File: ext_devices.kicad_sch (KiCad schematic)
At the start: 12 parts, among them CON1 MIKROBUS_HOST_CONN, J14 Conn_01x08_Female, J15 Conn_01x08_Female, U12 TXS0102DCU, U13 TXS0102DCU

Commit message: optimized component selection, assigned missing LCSC part numbers
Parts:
- C61, C62, C63, C64: footprint Capacitor_SMD:C_0805_2012Metric_Pad1.18x1.45mm_HandSolder -> Capacitor_SMD:C_0805_2012Metric
- D3: LCSC (none) -> C96235
- U12, U13: LCSC (none) -> C53434
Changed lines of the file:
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@@
     (property "Reference" "C64" (id 0) (at 130.81 128.27 90))
     (property "Value" "100nF" (id 1) (at 130.81 130.81 90))
-    (property "Footprint" "Capacitor_SMD:C_0805_2012Metric_Pad1.18x1.45mm_HandSolder" (id 2) (at 134.62 134.9248 0)
+    (property "Footprint" "Capacitor_SMD:C_0805_2012Metric" (id 2) (at 134.62 134.9248 0)
       (effects (font (size 1.27 1.27)) hide)
     )
@@
     (property "Reference" "C63" (id 0) (at 118.11 128.27 90))
     (property "Value" "100nF" (id 1) (at 118.11 130.81 90))
-    (property "Footprint" "Capacitor_SMD:C_0805_2012Metric_Pad1.18x1.45mm_HandSolder" (id 2) (at 121.92 134.9248 0)
+    (property "Footprint" "Capacitor_SMD:C_0805_2012Metric" (id 2) (at 121.92 134.9248 0)
       (effects (font (size 1.27 1.27)) hide)
     )
@@
     (property "Reference" "C62" (id 0) (at 62.865 128.27 90))
     (property "Value" "100nF" (id 1) (at 62.865 130.81 90))
-    (property "Footprint" "Capacitor_SMD:C_0805_2012Metric_Pad1.18x1.45mm_HandSolder" (id 2) (at 66.675 134.9248 0)
+    (property "Footprint" "Capacitor_SMD:C_0805_2012Metric" (id 2) (at 66.675 134.9248 0)
       (effects (font (size 1.27 1.27)) hide)
     )
@@
     )
     (property "Datasheet" "http://www.ti.com/lit/gpn/txs0102" (id 3) (at 124.46 152.908 0)
+      (effects (font (size 1.27 1.27)) hide)
+    )
+    (property "LCSC" "C53434" (id 4) (at 124.46 152.4 0)
       (effects (font (size 1.27 1.27)) hide)
     )
@@
     (property "Reference" "C61" (id 0) (at 45.085 128.27 90))
     (property "Value" "100nF" (id 1) (at 45.085 130.81 90))
-    (property "Footprint" "Capacitor_SMD:C_0805_2012Metric_Pad1.18x1.45mm_HandSolder" (id 2) (at 48.895 134.9248 0)
+    (property "Footprint" "Capacitor_SMD:C_0805_2012Metric" (id 2) (at 48.895 134.9248 0)
       (effects (font (size 1.27 1.27)) hide)
     )
@@
     )
     (property "Datasheet" "https://datasheet.lcsc.com/lcsc/1811061814_Nexperia-PMEG4050EP-115_C96235.pdf" (id 3) (at 192.405 36.83 0)
+      (effects (font (size 1.27 1.27)) hide)
+    )
+    (property "LCSC" "C96235" (id 4) (at 192.405 36.83 0)
       (effects (font (size 1.27 1.27)) hide)
     )
@@
       (effects (font (size 1.27 1.27)) hide)
     )
+    (property "LCSC" "C53434" (id 4) (at 53.34 152.4 0)
+      (effects (font (size 1.27 1.27)) hide)
+    )

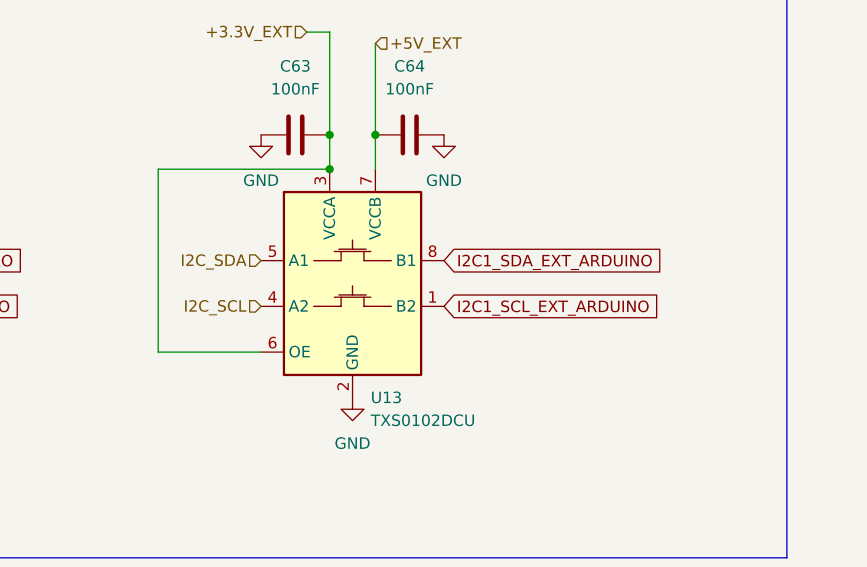
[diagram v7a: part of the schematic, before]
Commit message: added second level shifter to PCB
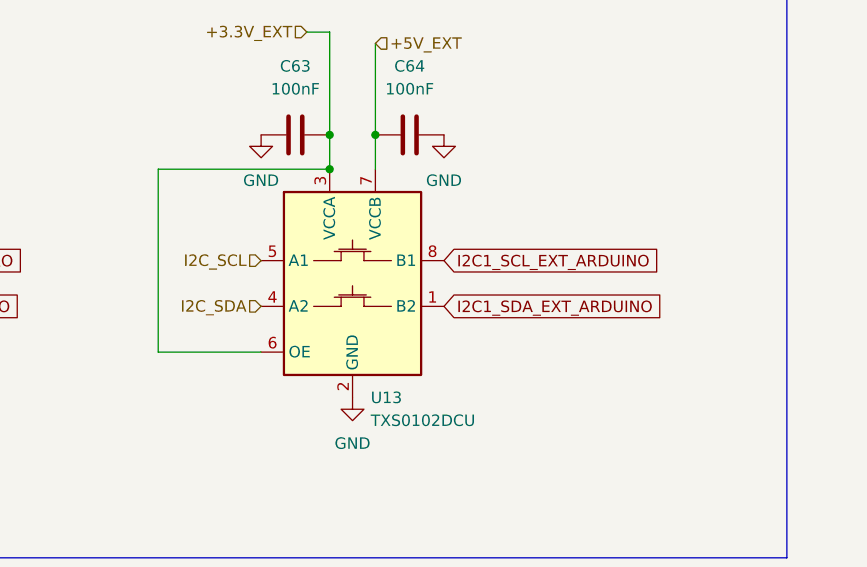
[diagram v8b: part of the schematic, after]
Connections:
- net I2C1_SCL_EXT_ARDUINO: now also U13.8 (B1); no longer U13.1 (B2)
- net I2C1_SDA_EXT_ARDUINO: now also U13.1 (B2); no longer U13.8 (B1)
- net I2C_SCL: now also U13.5 (A1); no longer U13.4 (A2)
- net I2C_SDA: now also U13.4 (A2); no longer U13.5 (A1)
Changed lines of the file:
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@@
     (effects (font (size 1.27 1.27)) (justify left bottom))
   )
-  (global_label "I2C1_SDA_EXT_ARDUINO" (shape input) (at 134.62 149.86 0) (fields_autoplaced)
-    (effects (font (size 1.27 1.27)) (justify left))
-    (property "Intersheet References" "${INTERSHEET_REFS}" (id 0) (at 159.3488 149.7806 0)
+  (global_label "I2C1_SDA_EXT_ARDUINO" (shape input) (at 134.62 154.94 0) (fields_autoplaced)
+    (effects (font (size 1.27 1.27)) (justify left))
+    (property "Intersheet References" "${INTERSHEET_REFS}" (id 0) (at 159.3488 154.8606 0)
       (effects (font (size 1.27 1.27)) (justify left) hide)
     )
@@
     )
   )
-  (global_label "I2C1_SCL_EXT_ARDUINO" (shape input) (at 134.62 154.94 0) (fields_autoplaced)
-    (effects (font (size 1.27 1.27)) (justify left))
-    (property "Intersheet References" "${INTERSHEET_REFS}" (id 0) (at 159.2883 154.8606 0)
+  (global_label "I2C1_SCL_EXT_ARDUINO" (shape input) (at 134.62 149.86 0) (fields_autoplaced)
+    (effects (font (size 1.27 1.27)) (justify left))
+    (property "Intersheet References" "${INTERSHEET_REFS}" (id 0) (at 159.2883 149.7806 0)
       (effects (font (size 1.27 1.27)) (justify left) hide)
     )
@@
     (effects (font (size 1.27 1.27)) (justify right))
   )
-  (hierarchical_label "I2C_SCL" (shape input) (at 114.3 154.94 180)
+  (hierarchical_label "I2C_SCL" (shape input) (at 114.3 149.86 180)
     (effects (font (size 1.27 1.27)) (justify right))
   )
@@
     (effects (font (size 1.27 1.27)) (justify right))
   )
-  (hierarchical_label "I2C_SDA" (shape input) (at 114.3 149.86 180)
-    (effects (font (size 1.27 1.27)) (justify right))
-  )
+  (hierarchical_label "I2C_SDA" (shape input) (at 114.3 154.94 180)
+    (effects (font (size 1.27 1.27)) (justify right))
+  )
